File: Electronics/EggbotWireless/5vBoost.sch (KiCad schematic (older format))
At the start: 11 parts, among them U9 LM2621

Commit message: change 5vboost inductor to smaller
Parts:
- L3: footprint Inductor_SMD:L_7.3x7.3_H4.5 -> Inductor_SMD:L_6.3x6.3_H3; Part (none) -> CKCS6028
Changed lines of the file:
@@
 F 0 "L3" V 3450 3500 50  0000 C CNN
 F 1 "6.8uH" V 3350 3500 50  0000 C CNN
-F 2 "Inductor_SMD:L_7.3x7.3_H4.5" H 3500 3500 50  0001 C CNN
+F 2 "Inductor_SMD:L_6.3x6.3_H3" H 3500 3500 50  0001 C CNN
 F 3 "~" H 3500 3500 50  0001 C CNN
+F 4 "CKCS6028" V 3500 3500 50  0001 C CNN "Part"
 	1    3500 3500
 	0    -1   -1   0

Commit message: [Board] fix some issues 1. change 5vboost output capacitor to 68 uF 2. change ATMega crystal to 12MHz
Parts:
- C21: value 10uF -> 68uF; footprint Capacitor_SMD:CP_Elec_4x5.4 -> Capacitor_SMD:CP_Elec_4x5.8
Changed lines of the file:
@@
 AR Path="/5E1045DA/5E217A35" Ref="C21"  Part="1"
 F 0 "C21" H 5818 3796 50  0000 L CNN
-F 1 "10uF" H 5818 3705 50  0000 L CNN
-F 2 "Capacitor_SMD:CP_Elec_4x5.4" H 5738 3600 50  0001 C CNN
+F 1 "68uF" H 5818 3705 50  0000 L CNN
+F 2 "Capacitor_SMD:CP_Elec_4x5.8" H 5738 3600 50  0001 C CNN
 F 3 "~" H 5700 3750 50  0001 C CNN
 	1    5700 3750

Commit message: TPS61023 - based 5v booster
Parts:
- removed C19: 22pF, Capacitor_SMD:C_0805_2012Metric_Pad1.15x1.40mm_HandSolder, symbol EggbotWireless-rescue:C-Device-Catfi-rescue
- removed C20: 100nF, Capacitor_SMD:C_0805_2012Metric_Pad1.15x1.40mm_HandSolder, symbol EggbotWireless-rescue:C-Device-Catfi-rescue
- removed D5: SSB43L, Diode_SMD:D_SMB_Handsoldering, symbol EggbotWireless-rescue:D_Schottky-Device
- removed R29: 200K, Resistor_SMD:R_0805_2012Metric_Pad1.15x1.40mm_HandSolder, symbol EggbotWireless-rescue:R-Device
- removed R30: 500, Resistor_SMD:R_0805_2012Metric_Pad1.15x1.40mm_HandSolder, symbol EggbotWireless-rescue:R-Device
- removed U9: LM2621, Package_SO:VSSOP-8_3.0x3.0mm_P0.65mm, symbol LM2621:LM2621
- added C? (x2): 10uF, Capacitor_SMD:C_0805_2012Metric_Pad1.15x1.40mm_HandSolder, symbol EggbotWireless-rescue:C-Device
- added U?: TPS61023, Package_TO_SOT_SMD:SOT-563, symbol tps61023:TPS61023
- C18: value 10uF -> 68uF; footprint Capacitor_SMD:CP_Elec_4x5.4 -> Capacitor_SMD:CP_Elec_4x5.8
- C21: value 68uF -> 220uF; footprint Capacitor_SMD:CP_Elec_4x5.8 -> Capacitor_SMD:CP_Elec_8x10.5
- L3: value 6.8uH -> 1uH; Part CKCS6028 -> SPM5030T-1R0M
- R23: value 50K -> 100K
- R28: value 150K -> 750K
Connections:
- wire segments 36 -> 30
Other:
- moved on the sheet: C18, C21, L3, R23, R28

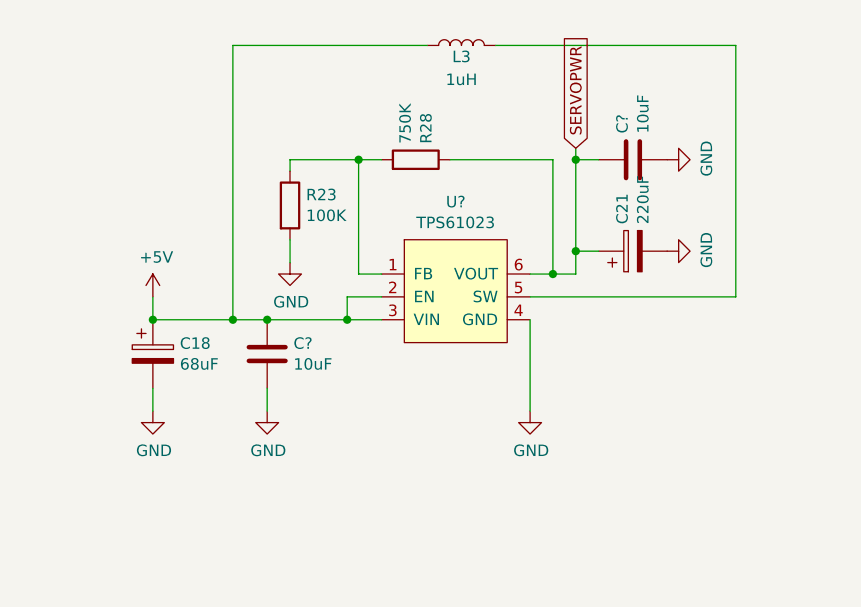
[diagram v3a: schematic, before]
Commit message: add all the new components to the board
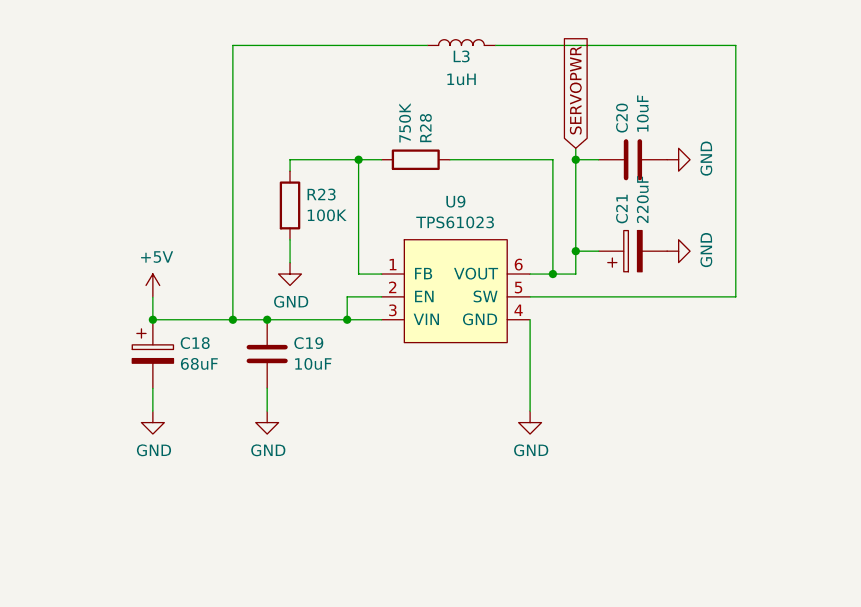
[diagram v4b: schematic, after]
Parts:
- gave numbers to parts that had none: 3
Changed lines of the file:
@@
 $EndComp
 $Comp
-L tps61023:TPS61023 U?
+L tps61023:TPS61023 U9
 U 1 1 5F047171
 P 4800 3600
-F 0 "U?" H 4825 3715 50  0000 C CNN
+F 0 "U9" H 4825 3715 50  0000 C CNN
 F 1 "TPS61023" H 4825 3624 50  0000 C CNN
 F 2 "Package_TO_SOT_SMD:SOT-563" H 4800 3600 50  0001 C CNN
@@
 	5000 2800 6050 2800
 $Comp
-L power:GND #PWR?
+L power:GND #PWR0159
 U 1 1 5F057A38
 P 4100 3750
-F 0 "#PWR?" H 4100 3500 50  0001 C CNN
+F 0 "#PWR0159" H 4100 3500 50  0001 C CNN
 F 1 "GND" H 4105 3577 50  0000 C CNN
 F 2 "" H 4100 3750 50  0001 C CNN
@@
 P 4000 4150
 AR Path="/5F074742" Ref="C?"  Part="1"
-AR Path="/5E1045DA/5F074742" Ref="C?"  Part="1"
-F 0 "C?" H 4115 4196 50  0000 L CNN
+AR Path="/5E1045DA/5F074742" Ref="C19"  Part="1"
+F 0 "C19" H 4115 4196 50  0000 L CNN
 F 1 "10uF" H 4115 4105 50  0000 L CNN
 F 2 "Capacitor_SMD:C_0805_2012Metric_Pad1.15x1.40mm_HandSolder" H 4038 4000 50  0001 C CNN
@@
 	4000 4000 4350 4000
 $Comp
-L power:GND #PWR?
+L power:GND #PWR0162
 U 1 1 5F077512
 P 4000 4400
-F 0 "#PWR?" H 4000 4150 50  0001 C CNN
+F 0 "#PWR0162" H 4000 4150 50  0001 C CNN
 F 1 "GND" H 4005 4227 50  0000 C CNN
 F 2 "" H 4000 4400 50  0001 C CNN
@@
 P 5600 3300
 AR Path="/5F078162" Ref="C?"  Part="1"
-AR Path="/5E1045DA/5F078162" Ref="C?"  Part="1"
-F 0 "C?" H 5715 3346 50  0000 L CNN
+AR Path="/5E1045DA/5F078162" Ref="C20"  Part="1"
+F 0 "C20" H 5715 3346 50  0000 L CNN
 F 1 "10uF" H 5715 3255 50  0000 L CNN
 F 2 "Capacitor_SMD:C_0805_2012Metric_Pad1.15x1.40mm_HandSolder" H 5638 3150 50  0001 C CNN
@@
 	5350 3700 5350 3800
 $Comp
-L power:GND #PWR?
+L power:GND #PWR0164
 U 1 1 5F07A4BB
 P 5750 3300
-F 0 "#PWR?" H 5750 3050 50  0001 C CNN
+F 0 "#PWR0164" H 5750 3050 50  0001 C CNN
 F 1 "GND" H 5755 3127 50  0000 C CNN
 F 2 "" H 5750 3300 50  0001 C CNN
